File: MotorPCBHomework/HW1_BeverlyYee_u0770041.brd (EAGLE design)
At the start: 50.4 x 26 mm, 20 parts, among them J1 CON-SOCJ-2155, U1 L298N, U2 LM75AIMX

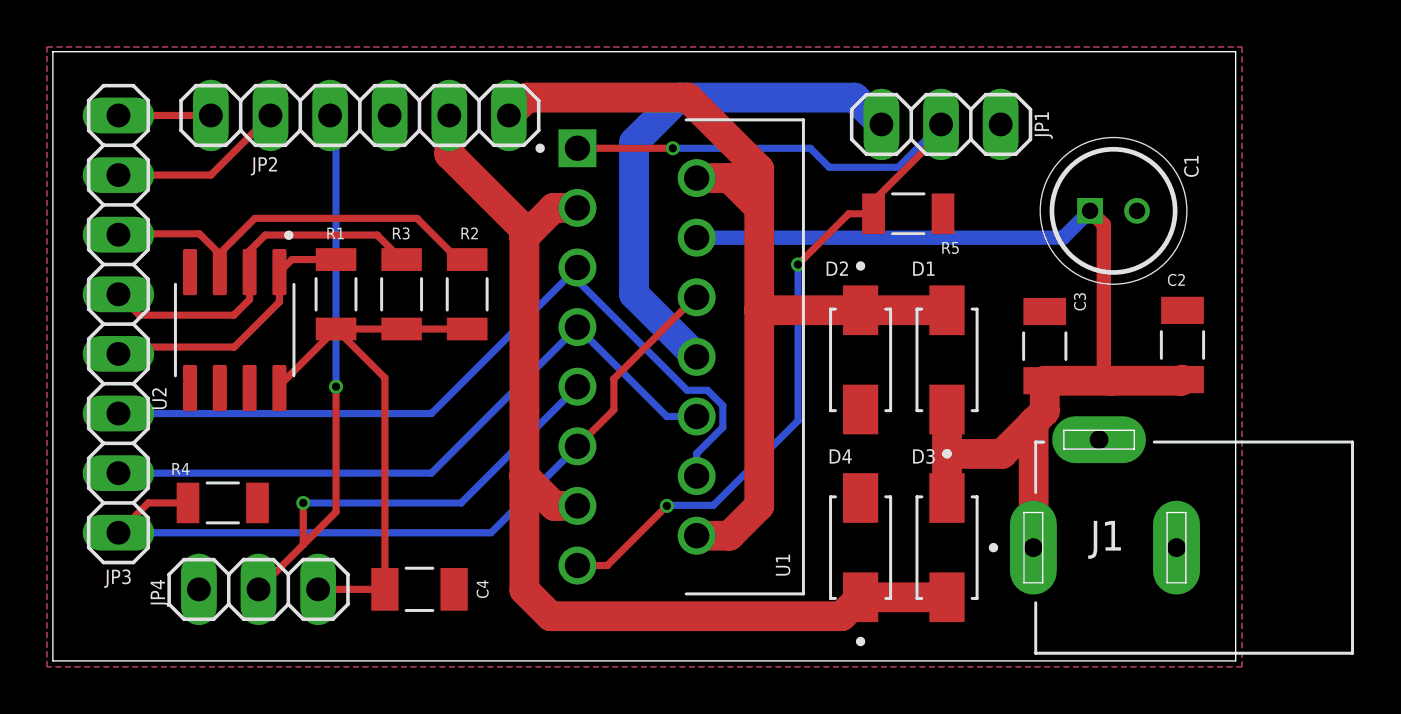
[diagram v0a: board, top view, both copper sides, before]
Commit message: Eliminate all airwires
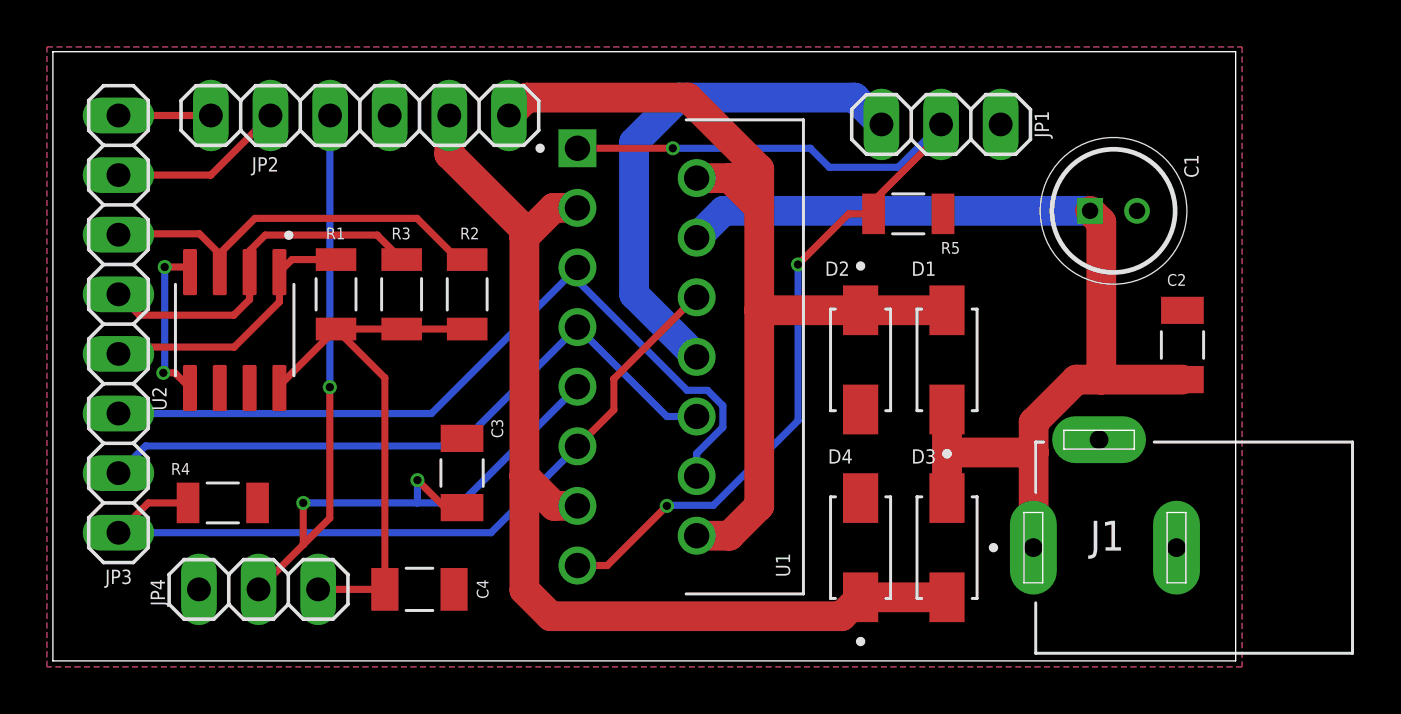
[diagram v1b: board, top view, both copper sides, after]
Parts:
- moved C3 25.4 mm to (48.2, 26.8)
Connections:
- new net 3.3V: C4.1, JP4.3, R1.2, R2.1, R3.2, U2.8
- new net 5V: C3.2, JP2.4, JP4.2, U1.9
- net VCC: no longer C3.2, C4.1, JP2.4, JP4.2, JP4.3, R1.2, R2.1, R3.2, U1.9, U2.8
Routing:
- net VCC: track 107.2 -> 44.6 mm, vias 2 -> 0
- net 5V: track 0.00 -> 40.3 mm, vias 0 -> 3
- net 3.3V: track 0.00 -> 23.9 mm
- net GND: track 22.1 -> 29.2 mm, vias 0 -> 2

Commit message: Add lab 3
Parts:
- moved R4 0.78 mm to (38.7, 25.9)
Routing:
- net ENABLE: track 33.1 -> 33.9 mm
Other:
- board text added: "+"
- board text added: "-"
- board text added: "3.3V"
- board text added: "5V"
- board text added: "BLK"
- board text added: "ENABLE"
- board text added: "ENAO"
- board text added: "ENBO"
- board text added: "GND"
- board text added: "IN1"
- board text added: "IN2"
- board text added: "OS"
- board text added: "RED"
- board text added: "SCL"
- board text added: "SDA"
- board text added: "SNSR"
